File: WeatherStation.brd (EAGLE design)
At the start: 30.5 x 44.5 mm, 20 parts, among them J1 EDISON_CONNECTOR_FULLMOUNTING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, J2 EDISON_CONNECTOR_FULLHEADER, U1 MCP73831

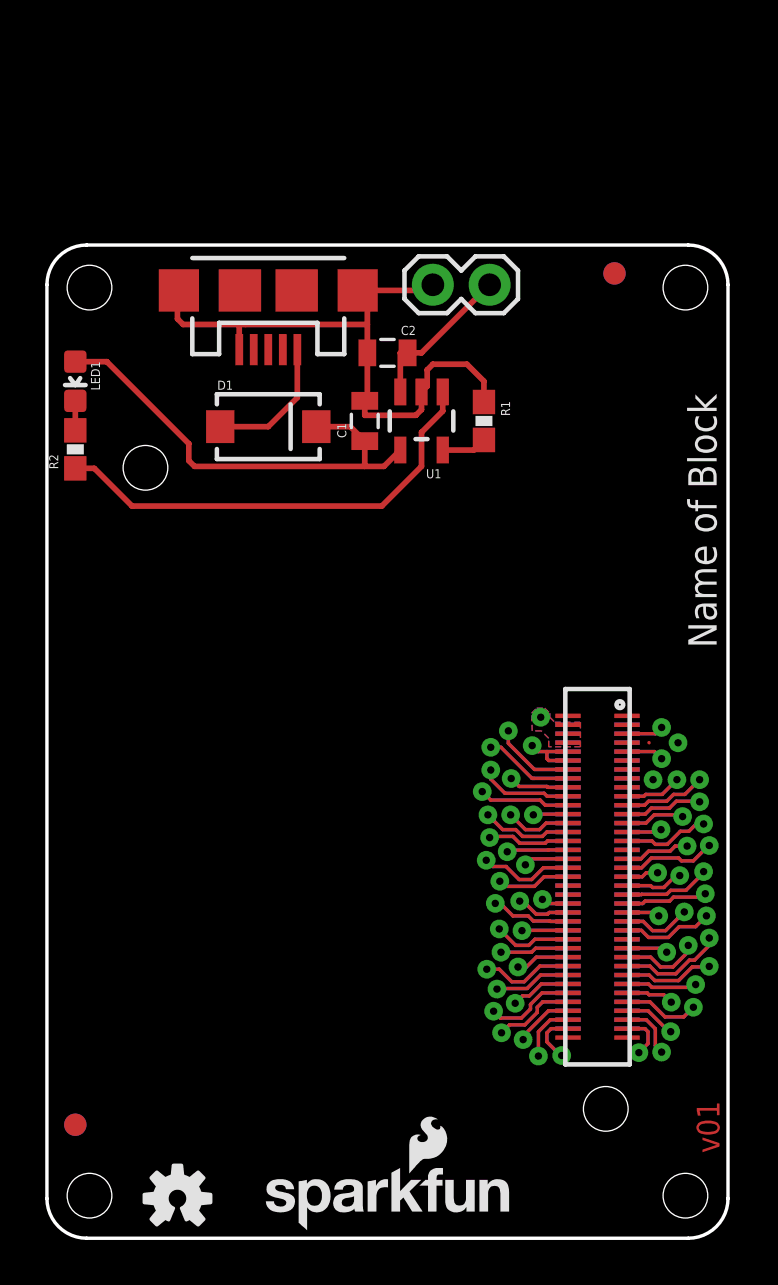
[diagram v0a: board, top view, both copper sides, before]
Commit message: extended board length
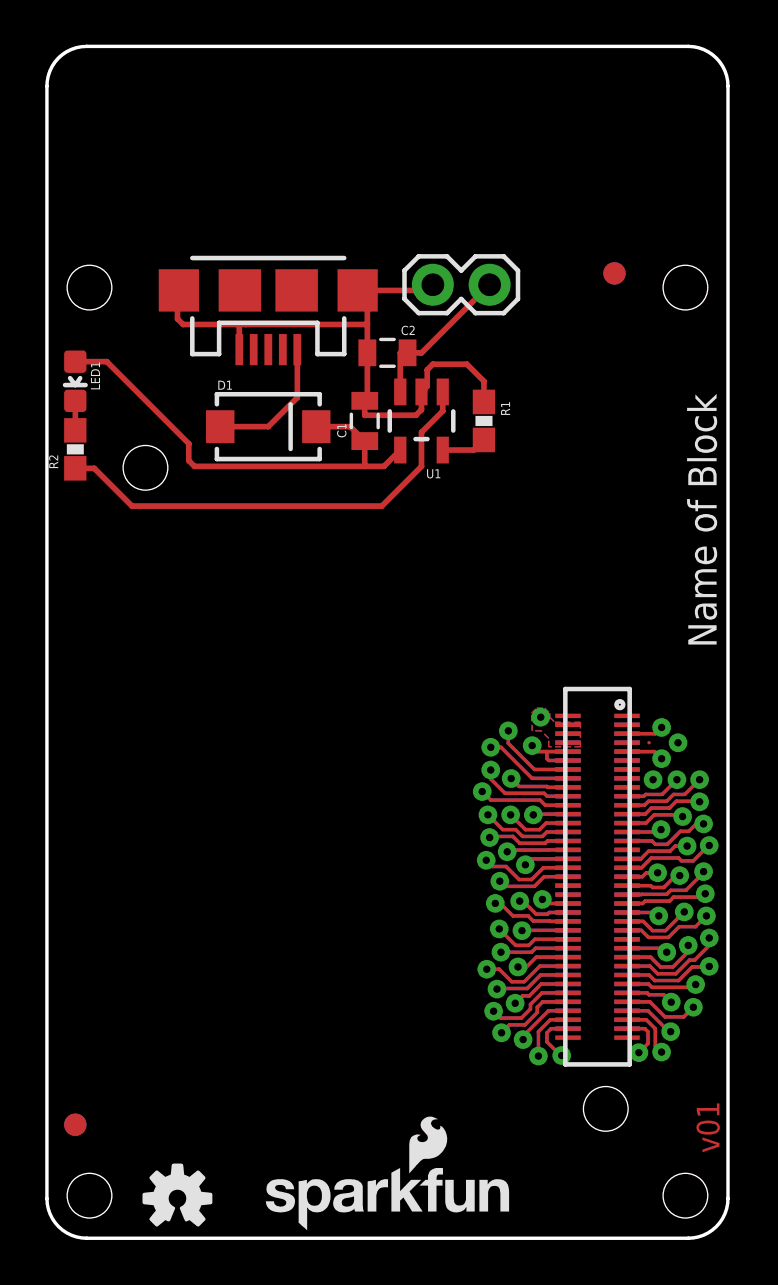
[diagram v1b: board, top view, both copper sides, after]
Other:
- board size 30.5 x 44.5 mm -> 30.5 x 53.3 mm
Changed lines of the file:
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@@
 <board>
 <plain>
-<wire x1="30.48" y1="42.672" x2="30.48" y2="1.778" width="0.1524" layer="20"/>
+<wire x1="30.48" y1="51.562" x2="30.48" y2="1.778" width="0.1524" layer="20"/>
 <wire x1="28.702" y1="0" x2="1.778" y2="0" width="0.1524" layer="20"/>
-<wire x1="0" y1="1.778" x2="0" y2="42.672" width="0.1524" layer="20"/>
+<wire x1="0" y1="1.778" x2="0" y2="51.562" width="0.1524" layer="20"/>
 <text x="29.21" y="-13.97" size="1.6764" layer="51" ratio="15">Engineer</text>
 <hole x="28.575" y="1.905" drill="2"/>
@@
 <text x="31.115" y="22.225" size="1.27" layer="51" rot="R270" align="bottom-center">Nothing goes here...  I mean it.</text>
 <text x="29.972" y="26.416" size="1.27" layer="21" font="vector" ratio="15" rot="R90">Name of Block</text>
-<wire x1="1.778" y1="44.45" x2="28.702" y2="44.45" width="0.1524" layer="20"/>
+<wire x1="1.778" y1="53.34" x2="28.702" y2="53.34" width="0.1524" layer="20"/>
 <wire x1="30.48" y1="46.99" x2="30.48" y2="53.34" width="0.254" layer="51"/>
 <wire x1="30.48" y1="53.34" x2="0" y2="53.34" width="0.254" layer="51"/>
@@
 <wire x1="30.48" y1="1.778" x2="28.702" y2="0" width="0.1524" layer="20" curve="-90"/>
 <wire x1="1.778" y1="0" x2="0" y2="1.778" width="0.1524" layer="20" curve="-90"/>
-<wire x1="0" y1="42.672" x2="1.778" y2="44.45" width="0.1524" layer="20" curve="-90"/>
-<wire x1="28.702" y1="44.45" x2="30.48" y2="42.672" width="0.1524" layer="20" curve="-90"/>
+<wire x1="0" y1="51.562" x2="1.778" y2="53.34" width="0.1524" layer="20" curve="-90"/>
+<wire x1="28.702" y1="53.34" x2="30.48" y2="51.562" width="0.1524" layer="20" curve="-90"/>
 <text x="15.24" y="53.975" size="1.27" layer="51" align="bottom-center">Max Board Length</text>
 <dimension x1="28.575" y1="1.905" x2="1.905" y2="1.905" x3="15.24" y3="-2.54" textsize="1.27" textratio="10" layer="51" dtype="horizontal" unit="inch"/>
@@
 <signal name="GND">
 <polygon width="0.1778" layer="16" spacing="0.254" rank="6">
-<vertex x="30.48" y="42.672"/>
+<vertex x="30.48" y="51.562"/>
 <vertex x="30.48" y="1.778" curve="-90"/>
 <vertex x="28.702" y="0"/>
 <vertex x="1.778" y="0" curve="-90"/>
 <vertex x="0" y="1.778"/>
-<vertex x="0" y="42.672" curve="-90"/>
-<vertex x="1.778" y="44.45"/>
-<vertex x="28.702" y="44.45" curve="-90"/>
+<vertex x="0" y="51.562" curve="-90"/>
+<vertex x="1.524" y="53.34"/>
+<vertex x="28.448" y="53.34" curve="-90"/>
 </polygon>
 <polygon width="0.1778" layer="1" spacing="0.254" rank="6">
@@
 <vertex x="1.778" y="0" curve="-90"/>
 <vertex x="0" y="1.778"/>
-<vertex x="0" y="42.672" curve="-90"/>
-<vertex x="1.778" y="44.45"/>
-<vertex x="28.702" y="44.45" curve="-90"/>
-<vertex x="30.48" y="42.672"/>
+<vertex x="0" y="51.562" curve="-90"/>
+<vertex x="1.778" y="53.34"/>
+<vertex x="28.702" y="53.34" curve="-90"/>
+<vertex x="30.48" y="51.562"/>
 </polygon>
 <via x="28.2448" y="22.1742" extent="1-16" drill="0.3302"/>

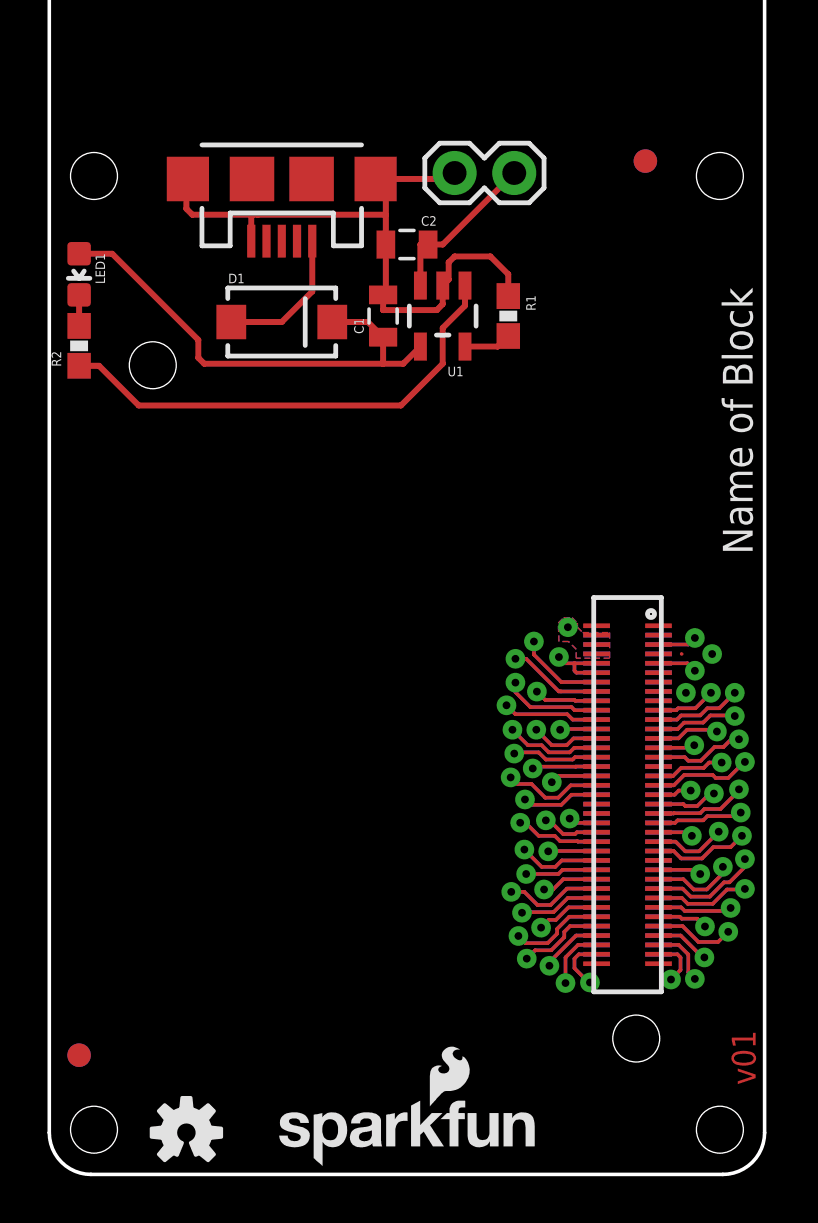
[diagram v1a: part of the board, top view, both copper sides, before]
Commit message: moved charge circuit and cleaned up some
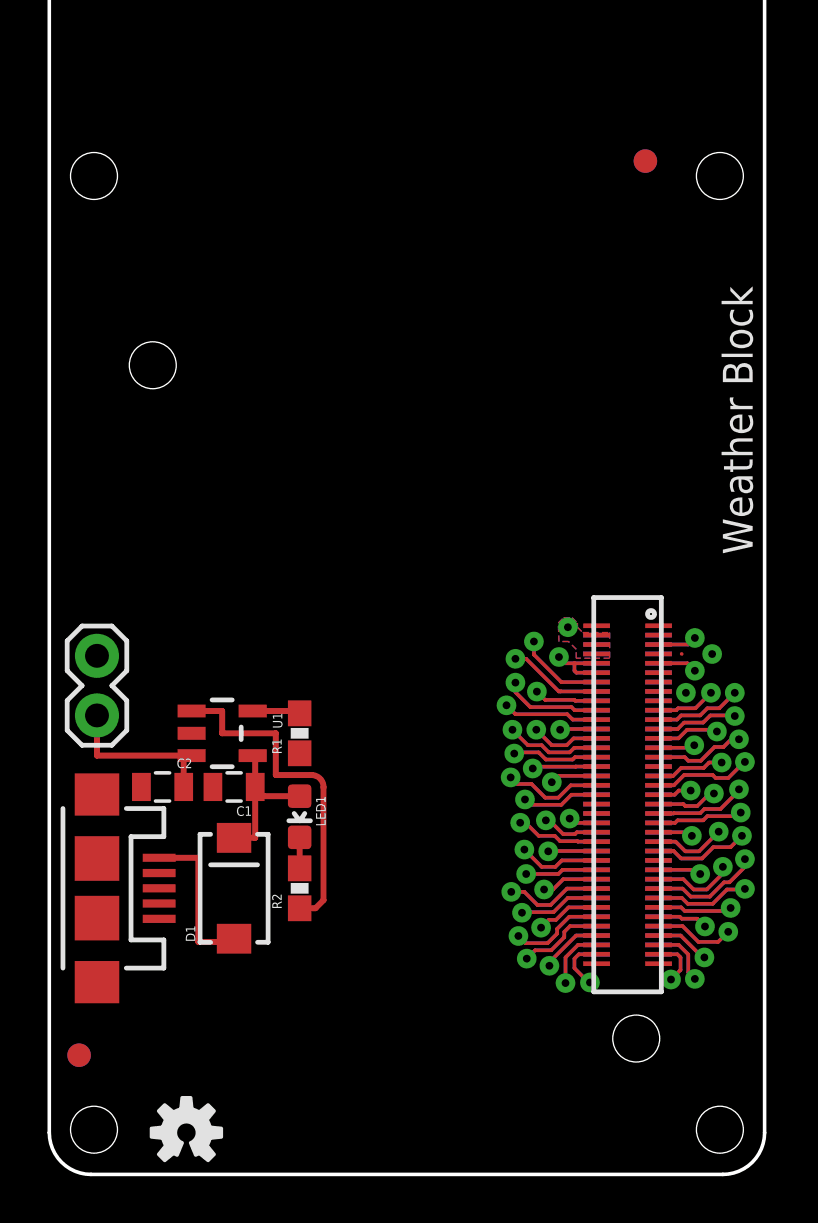
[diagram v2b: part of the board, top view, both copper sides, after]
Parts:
- removed LOGO3, LOGO4: SFE_LOGO_NAME_FLAME.1_INCH, SparkFun-Aesthetics:SFE_LOGO_NAME_FLAME_.1
- moved JP1 31.2 mm to (2.03, 12.2), turned to 270 degrees
- moved JP2 25.6 mm to (2.03, 22.1), turned to 270 degrees
- moved C2 25.4 mm to (4.83, 16.5)
- moved LED1 25.0 mm to (10.7, 15.2)
- moved R2 25.0 mm to (10.7, 12.2)
- moved D1 24.2 mm to (7.87, 12.2), turned to 90 degrees
- moved C1 21.0 mm to (7.87, 16.5), turned to 180 degrees
- moved U1 20.1 mm to (7.37, 18.8), turned to 270 degrees
- moved R1 19.9 mm to (10.7, 18.8), turned to 90 degrees
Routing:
- net GND: track 29.0 -> 0.01 mm
- net N$2: track 20.8 -> 6.51 mm
- net N$5: track 20.7 -> 14.5 mm
- net N$1: track 6.13 -> 6.91 mm
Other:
- board text added: "Weather Block"
- board text removed: "4xM2.0"
- board text removed: "LEDs & User Switches/Buttons go here"
- board text removed: "Max Board Length"
- board text removed: "Name of Block"
- board text removed: "Nothing goes here... I mean it."
- board text removed: "User Interface/Connectors"
- board text removed: "v01"
